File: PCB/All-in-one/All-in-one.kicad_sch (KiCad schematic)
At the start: 82 parts, among them J1 HIGH VOLTAGE, J10 SWD, J2 LOW VOLTAGE, J3 Micro_SD_Card_Det, J4 USB_C_Receptacle_USB2.0, J5 GPIO, J6 Conn_01x02, J7 Conn_01x02, J8 I2C_EXT, J9 UART_EXT, Q1 AO3401A, SW1 SW_DP3T, SW2 SW_Push, SW3 SW_Push, U1 TPS563201DDCR, U2 NCP114AMX330TCG, U3 STM32F401CDUx, U4 BMP280, U5 MPU-6050, U6 USBLC6-2P6, U7 MT9700, U8 MT9700, Y1 25MHz 12pF

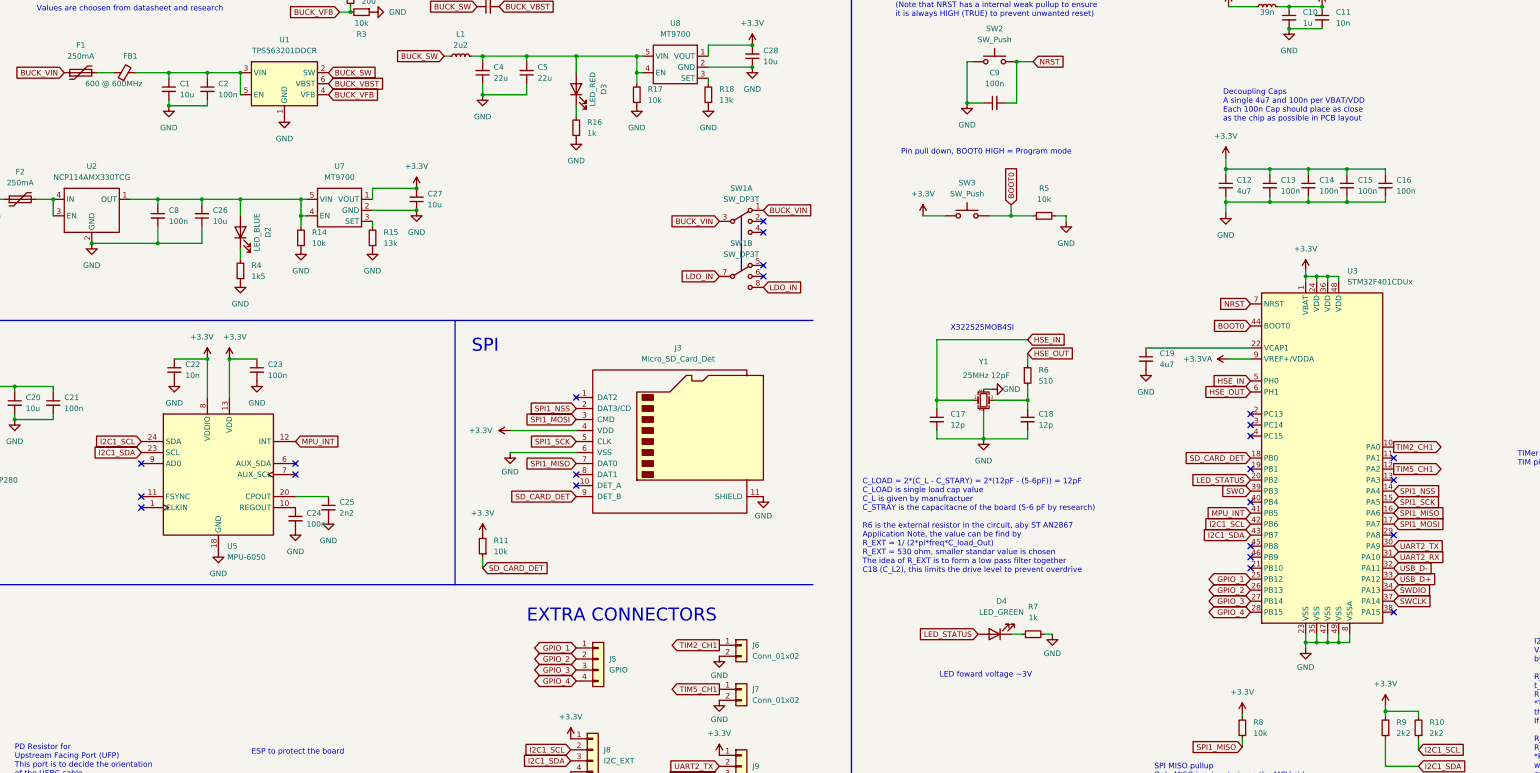
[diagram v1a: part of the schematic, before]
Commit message: Ver X01 PCB Routing Completed -  PCB is completed and all MFG files are exported - gbr files are uploaded to JLCPCB for quoting - All parts needed to be sourced - Encounterd some bug at using CubeIDE
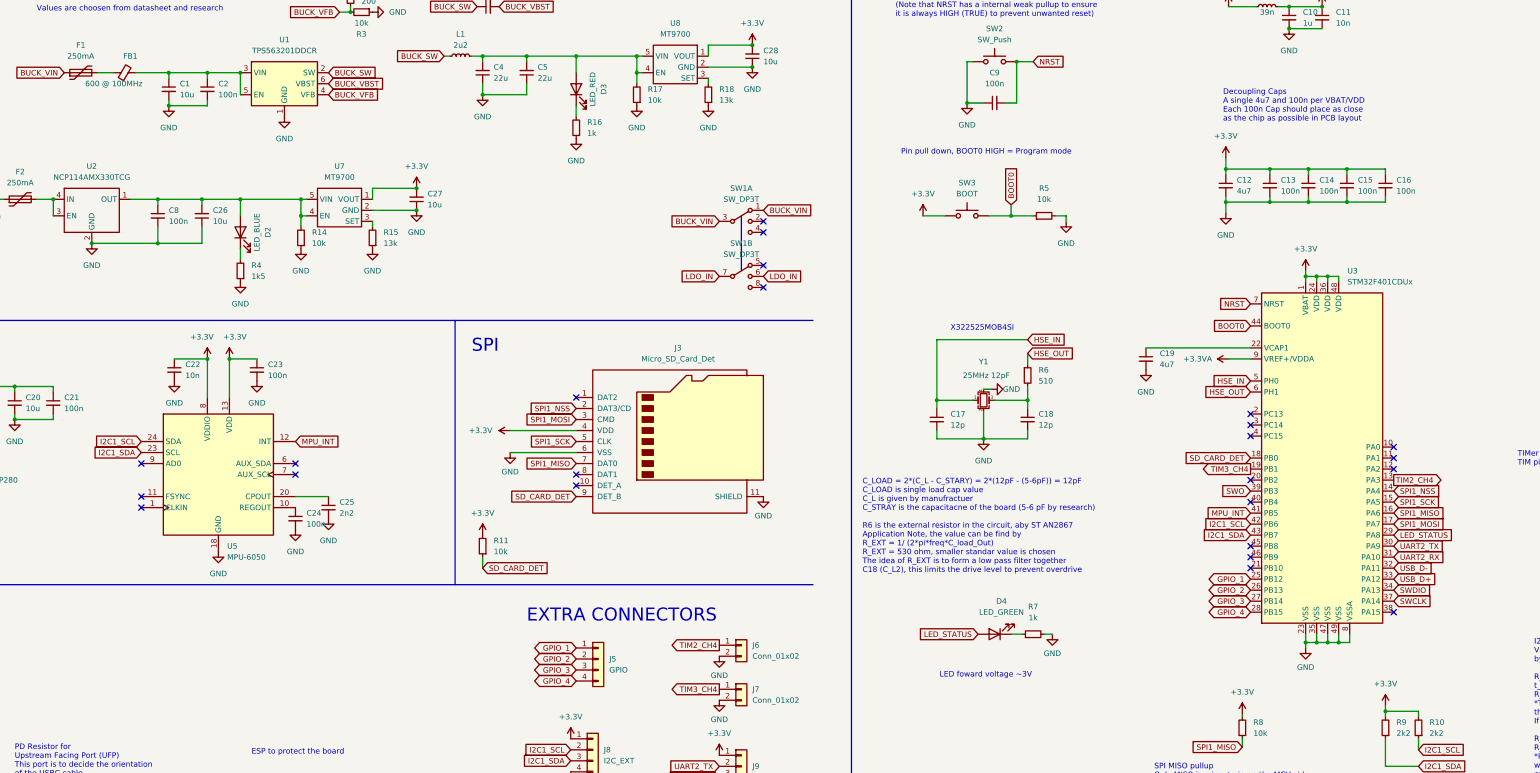
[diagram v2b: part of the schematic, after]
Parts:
- C1, C6: JLCPCB Part# (none) -> C13585
- C10: JLCPCB Part# (none) -> C15849
- C11, C22: JLCPCB Part# (none) -> C15195
- C12, C19: JLCPCB Part# (none) -> C19666
- C13, C14, C15, C16, C21, C23, C24, C9: JLCPCB Part# (none) -> C307331
- C17, C18: JLCPCB Part# (none) -> C1547
- C2: footprint Capacitor_SMD:C_0805_2012Metric -> Capacitor_SMD:C_1206_3216Metric; JLCPCB Part# (none) -> C24497
- C20: JLCPCB Part# (none) -> C96446
- C25: JLCPCB Part# (none) -> C1531
- C26, C27, C28: JLCPCB Part# (none) -> C15850
- C3, C7, C8: JLCPCB Part# (none) -> C28233
- C4, C5: JLCPCB Part# (none) -> C12891
- D1: JLCPCB Part# (none) -> C8598
- D2: JLCPCB Part# (none) -> C72041
- D3: JLCPCB Part# (none) -> C2286
- D4: footprint LED_SMD:LED_0402_1005Metric -> LED_SMD:LED_0603_1608Metric; JLCPCB Part# (none) -> C87326
- F1, F2: JLCPCB Part# (none) -> C269113; PART ID (none) -> SMD1206B025TF/24
- FB1: value 600 @ 600MHz -> 600 @ 100MHz; JLCPCB Part# (none) -> C73732
- L1: JLCPCB Part# (none) -> C135262
- L2: JLCPCB Part# (none) -> C86063
- Q1: JLCPCB Part# (none) -> C15127
- R1: JLCPCB Part# (none) -> C21117
- R2: JLCPCB Part# (none) -> C22975
- R4: JLCPCB Part# (none) -> C22843
- R6: JLCPCB Part# (none) -> C25123
- SW3: value SW_Push -> BOOT
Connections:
- net +BATT: now also SW1.6; no longer SW1.8
- net LED_STATUS: now also U3.29 (PA8); no longer U3.20 (PB2)
- net TIM2_CH4: now reaches U3.13 (PA3)
- net TIM2_CH4: now also J6.1 (Pin_1)
- net TIM3_CH4: now reaches U3.19 (PB1)
- net TIM3_CH4: now also J7.1 (Pin_1)
- net TIM2_CH1: no longer names the net of U3.10 (PA0)
- net TIM2_CH1: no longer J6.1 (Pin_1)
- net TIM5_CH1: no longer names the net of U3.12 (PA2)
- net TIM5_CH1: no longer J7.1 (Pin_1)

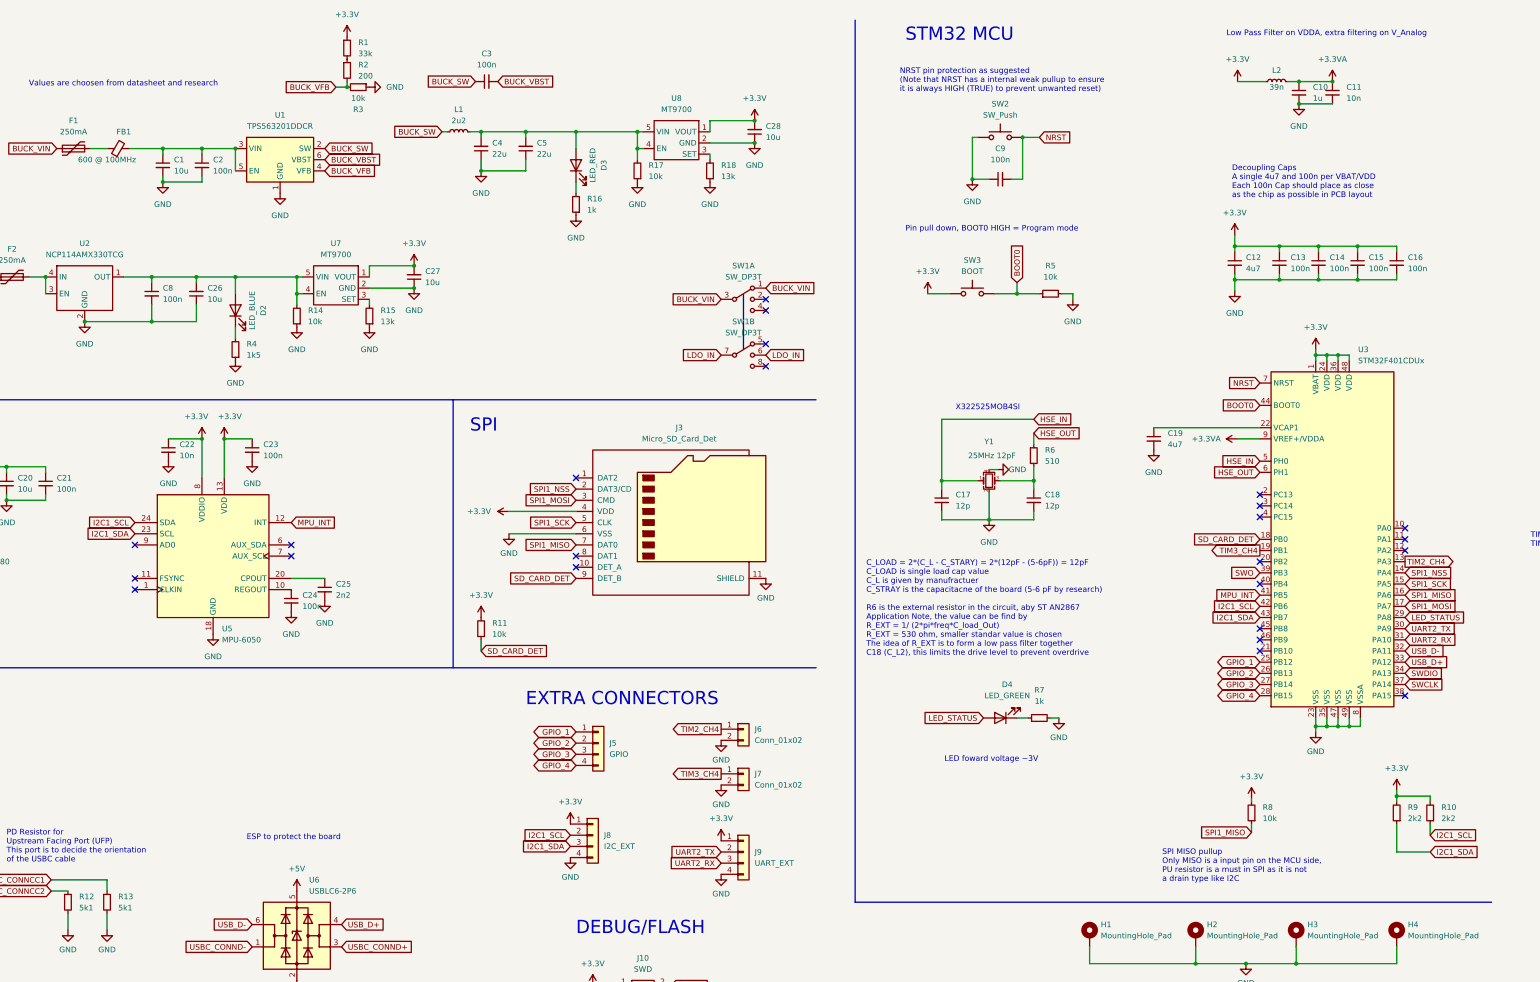
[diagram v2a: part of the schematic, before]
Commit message: Production Files Updated - Sent to JLCPCB for manufracturing - No SMD parts can be shipped with the order, to reduce the cost, it is most likely that a pre-assembled PCB will be ordered
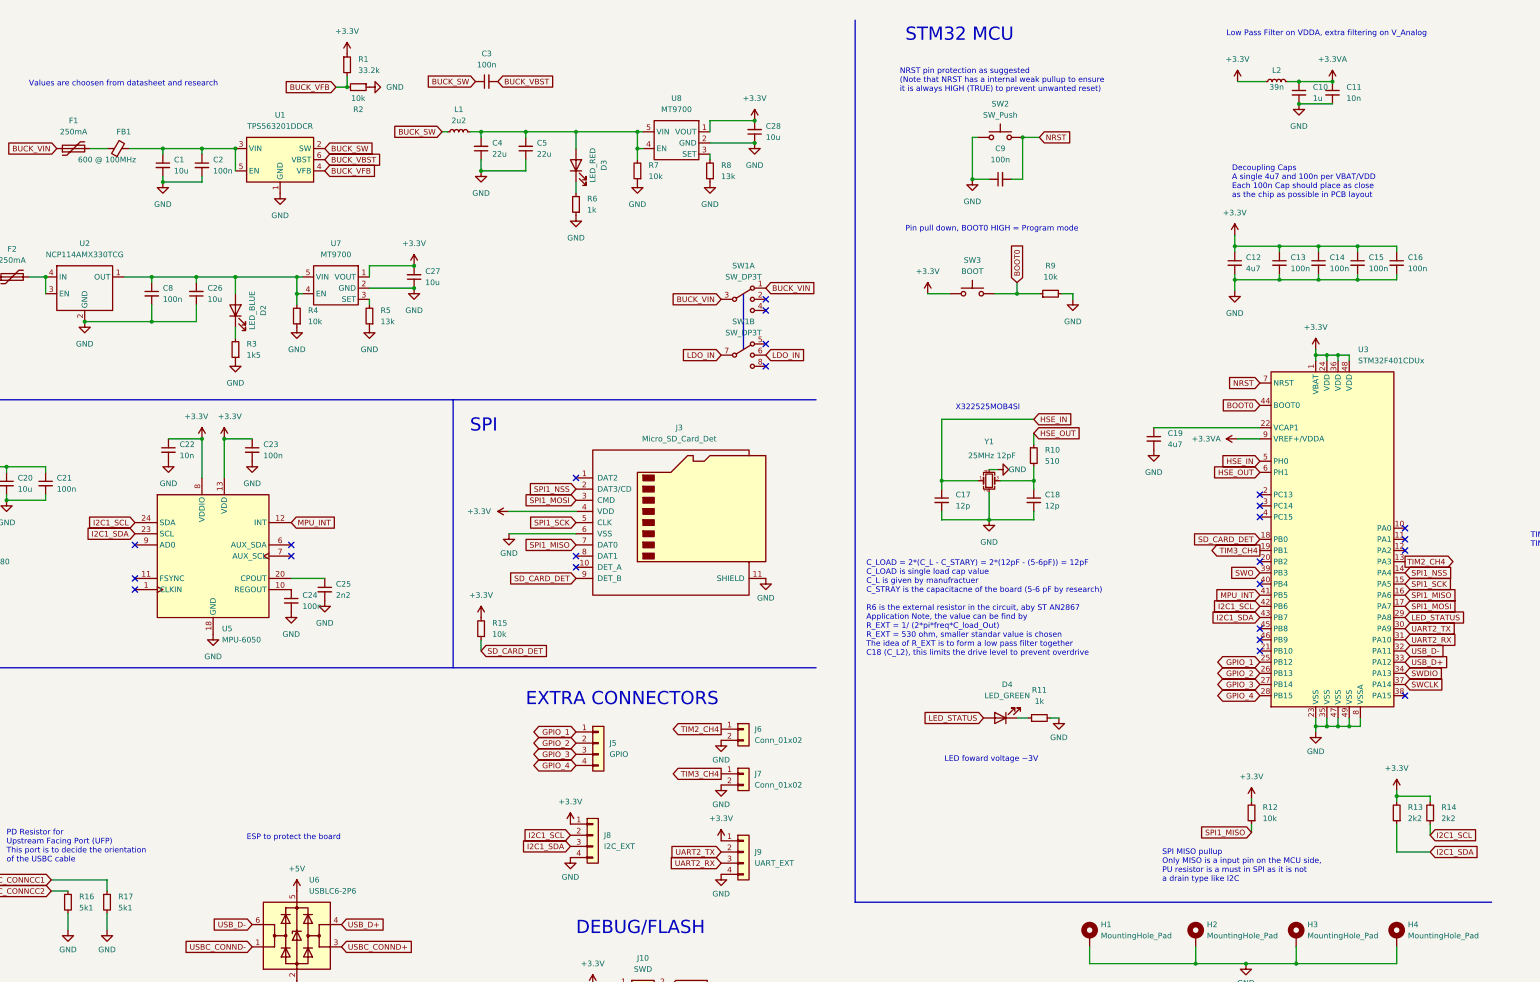
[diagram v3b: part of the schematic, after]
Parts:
- removed R2: 200, Resistor_SMD:R_0603_1608Metric, symbol Device:R_Small
- C1, C6: LCSC (none) -> C13585; LCSC Part (none) -> C13585
- C10: LCSC (none) -> C15849; LCSC Part (none) -> C15849
- C11, C22: LCSC (none) -> C15195; LCSC Part (none) -> C15195
- C12, C19: LCSC (none) -> C19666; LCSC Part (none) -> C19666
- C13, C14, C15, C16, C21, C23, C24, C9: LCSC (none) -> C307331; LCSC Part (none) -> C307331
- C17, C18: LCSC (none) -> C1547; LCSC Part (none) -> C1547
- C2: LCSC (none) -> C24497; LCSC Part (none) -> C24497
- C20: LCSC (none) -> C96446; LCSC Part (none) -> C96446
- C25: LCSC (none) -> C1531; LCSC Part (none) -> C1531
- C26, C27, C28: LCSC (none) -> C15850; LCSC Part (none) -> C15850
- C3, C7, C8: LCSC (none) -> C28233; LCSC Part (none) -> C28233
- C4, C5: LCSC (none) -> C12891; LCSC Part (none) -> C12891
- D1: LCSC (none) -> C8598; LCSC Part (none) -> C8598
- D2: LCSC (none) -> C72041; LCSC Part (none) -> C72041
- D3: LCSC (none) -> C2286; LCSC Part (none) -> C2286
- D4: LCSC (none) -> C87326; LCSC Part (none) -> C87326
- F1, F2: LCSC (none) -> C269113; LCSC Part (none) -> C269113
- FB1: LCSC (none) -> C73732; LCSC Part (none) -> C73732
- L1: LCSC (none) -> C135262; LCSC Part (none) -> C135262
- L2: LCSC (none) -> C86063; LCSC Part (none) -> C86063
- Q1: LCSC (none) -> C15127; LCSC Part (none) -> C15127
- R1: value 33k -> 33.2k; LCSC (none) -> C23003; LCSC Part (none) -> C23003
- R10: renamed from R6; LCSC (none) -> C25123; LCSC Part (none) -> C25123
- R11: renamed from R7; JLCPCB Part# (none) -> C21190; LCSC (none) -> C21190; LCSC Part (none) -> C21190
- R12: renamed from R8; JLCPCB Part# (none) -> C25744; LCSC (none) -> C25744; LCSC Part (none) -> C25744
- R13: renamed from R9; JLCPCB Part# (none) -> C4190; LCSC (none) -> C4190; LCSC Part (none) -> C4190
- R14: renamed from R10; JLCPCB Part# (none) -> C4190; LCSC (none) -> C4190; LCSC Part (none) -> C4190
- R15: renamed from R11; JLCPCB Part# (none) -> C25744; LCSC (none) -> C25744; LCSC Part (none) -> C25744
- R16: renamed from R12; JLCPCB Part# (none) -> C25905; LCSC (none) -> C25905; LCSC Part (none) -> C25905
- R17: renamed from R13; JLCPCB Part# (none) -> C25905; LCSC (none) -> C25905; LCSC Part (none) -> C25905
- R2: renamed from R3; JLCPCB Part# (none) -> C25804; LCSC (none) -> C25804; LCSC Part (none) -> C25804
- R3: renamed from R4; LCSC (none) -> C22843; LCSC Part (none) -> C22843
- R4: renamed from R14; JLCPCB Part# (none) -> C25804; LCSC (none) -> C25804; LCSC Part (none) -> C25804
- R5: renamed from R15; JLCPCB Part# (none) -> C22797; LCSC (none) -> C22797; LCSC Part (none) -> C22797
- R6: renamed from R16; JLCPCB Part# (none) -> C21190; LCSC (none) -> C21190; LCSC Part (none) -> C21190
- R7: renamed from R17; JLCPCB Part# (none) -> C25804; LCSC (none) -> C25804; LCSC Part (none) -> C25804
- R8: renamed from R18; JLCPCB Part# (none) -> C22797; LCSC (none) -> C22797; LCSC Part (none) -> C22797
- R9: renamed from R5; JLCPCB Part# (none) -> C25744; LCSC (none) -> C25744; LCSC Part (none) -> C25744
- SW1: JLCPCB Part# (none) -> C145841; LCSC (none) -> C145841; LCSC Part (none) -> C145841
- SW2, SW3: JLCPCB Part# (none) -> C843669; LCSC (none) -> C843669; LCSC Part (none) -> C843669
- U1: JLCPCB Part# (none) -> C116592; LCSC (none) -> C116592; LCSC Part (none) -> C116592
- U2: JLCPCB Part# (none) -> C133056; LCSC (none) -> C133056; LCSC Part (none) -> C133056
- U6: JLCPCB Part# (none) -> C2827693; LCSC (none) -> C2827693; LCSC Part (none) -> C2827693
- U7, U8: JLCPCB Part# (none) -> C89855; LCSC (none) -> C89855; LCSC Part (none) -> C89855
- Y1: JLCPCB Part# (none) -> C9006; LCSC (none) -> C9006; LCSC Part (none) -> C9006
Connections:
- net BUCK_VFB: now also R1.2
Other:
- moved on the sheet: R1

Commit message: Updated Circuit - Based on the new parts supplier LCSC, better components can be found - PCB is updated according to the new components
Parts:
- removed C26, C27, C28: 10u, Capacitor_SMD:C_0805_2012Metric, symbol Device:C_Small
- removed C4, C5: 22u, Capacitor_SMD:C_1206_3216Metric, symbol Device:C_Small
- removed C6: 10u, Capacitor_SMD:C_1206_3216Metric, symbol Device:C_Small
- removed C7, C8: 100n, Capacitor_SMD:C_0805_2012Metric, symbol Device:C_Small
- removed D2: LED_BLUE, LED_SMD:LED_0603_1608Metric, symbol Device:LED
- removed D3: LED_RED, LED_SMD:LED_0603_1608Metric, symbol Device:LED
- removed F2: 250mA, Fuse:Fuse_1206_3216Metric, symbol Device:Polyfuse
- removed J2: LOW VOLTAGE, TerminalBlock_TE-Connectivity:TerminalBlock_TE_282834-2_1x02_P2.54mm_Horizontal, symbol Connector:Screw_Terminal_01x02
- removed R5, R8: 13k, Resistor_SMD:R_0603_1608Metric, symbol Device:R_Small
- removed R6: 1k, Resistor_SMD:R_0603_1608Metric, symbol Device:R_Small
- removed R7: 10k, Resistor_SMD:R_0603_1608Metric, symbol Device:R_Small
- removed SW1: SW_DP3T, All-in-one-custom:K3-2336D-F1, symbol Switch:SW_DP3T
- removed U1: TPS563201DDCR, Package_TO_SOT_SMD:SOT-23-6, symbol Regulator_Switching:TPS563200
- removed U2: NCP114AMX330TCG, Package_DFN_QFN:UDFN-4-1EP_1x1mm_P0.65mm_EP0.48x0.48mm, symbol All-in-one_custom:NCP114AMX330TCG
- removed U7, U8: MT9700, Package_TO_SOT_SMD:SOT-23-5, symbol All-in-one_custom:MT9700
- added D2: LED_RED, LED_SMD:LED_0603_1608Metric, symbol Device:LED_Small
- added U1: TPMP1470, Package_TO_SOT_SMD:SOT-23-6, symbol All-in-one_custom:TPMP1470
- C1: value 10u -> 22u; JLCPCB Part# C13585 -> (none); LCSC C13585 -> C12891; LCSC Part C13585 -> (none)
- C2: value 100n -> 1u; footprint Capacitor_SMD:C_1206_3216Metric -> Capacitor_SMD:C_0805_2012Metric; JLCPCB Part# C24497 -> (none); LCSC C24497 -> C2798196; LCSC Part C24497 -> (none)
- C3: value 100n -> 22u; footprint Capacitor_SMD:C_0805_2012Metric -> Capacitor_SMD:C_1206_3216Metric; JLCPCB Part# C28233 -> (none); LCSC C28233 -> C12891; LCSC Part C28233 -> (none)
- D3: renamed from D4; LCSC C87326 -> C965805
- L1: value 2u2 -> 22u; footprint All-in-one-custom:SMNR4020-2.2UH -> All-in-one-custom:MPIT8040; JLCPCB Part# C135262 -> (none); LCSC C135262 -> C281320; LCSC Part C135262 -> (none); PART ID SMNR4020-2.2UH -> (none)
- R1: value 33.2k -> 75k; JLCPCB Part# C21117 -> (none); LCSC C23003 -> C18671; LCSC Part C23003 -> (none)
- R2: value 10k -> 40k2; JLCPCB Part# C25804 -> (none); LCSC C25804 -> C25893; LCSC Part C25804 -> (none)
- R3: value 1k5 -> 13k; JLCPCB Part# C22843 -> (none); LCSC C22843 -> C2907101; LCSC Part C22843 -> (none)
- R4: value 10k -> 13k; JLCPCB Part# C25804 -> (none); LCSC C25804 -> C2907101; LCSC Part C25804 -> (none)
- renumbered C15 to C10, C16 to C11, C17 to C12, C18 to C13, C19 to C14, C20 to C15, C21 to C16, C22 to C17, C23 to C18, C24 to C19, C25 to C20, C9 to C4, C10 to C5, C11 to C6, C12 to C7, C13 to C8, C14 to C9, J3 to J2, J4 to J3, J8 to J4, J10 to J6, J6 to J7, J7 to J8, R14 to R10, R15 to R11, R16 to R12, R17 to R13, R9 to R5, R10 to R6, R11 to R7, R12 to R8, R13 to R9, SW2 to SW1, SW3 to SW2, U3 to U2, U4 to U3, U5 to U4, U6 to U5
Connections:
- net BUCK_VBST is gone; now on net GND: C3.2
- net +3.3V: now also C3.1, L1.2, R2.1, D2.2 (A); no longer R1.1
- net GND: now also R3.2, R4.2, U1.1 (GND); no longer C2.2, R2.1, R3.1, R4.1
- net at C1.1, FB1.2: now also U1.3 (IN), U1.5 (EN); no longer C2.1
- net BUCK_SW: no longer names the net of L1.1
- net BUCK_SW: now also C2.1, U1.2 (SW/LX); no longer C3.1
- net BUCK_VFB: no longer names the net of R1.2, R2.2
- net BUCK_VFB: now also R3.1
- net BUCK_VIN: no longer names the net of D1.1 (K), F1.1, Q1.2 (S)
- new net: C2.2, U1.6 (BS)
- new net: R1.1, U1.4 (FB)
- new net: D2.1 (K), R4.1
- no-connect marks 28 -> 24
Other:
- note added: "Feed back voltage reference = 0.8V The value chosen is the recommended values, by datasheet, R1 = 10k will give the best transient response, it is worth to test a circuit with R1 = 10k"
- moved on the sheet: D1, F1, FB1, J1, Q1, R5, SW2
